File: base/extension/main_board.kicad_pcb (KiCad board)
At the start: 2 copper layers, 66.5 x 44 mm, 60 parts, among them IC1 TMC2209-LA-T, IC2 TMC2209-LA-T, IC3 TMC2209-LA-T, J1 USB_C_Receptacle_USB2.0_16P, J2 Conn_02x20_Odd_Even, J3 2-1734248-0, J4 Conn_01x02, J5 2-1734248-0, U1 LM7805_TO263, U2 MCP1700T-3302E/TT, U3 CH224K

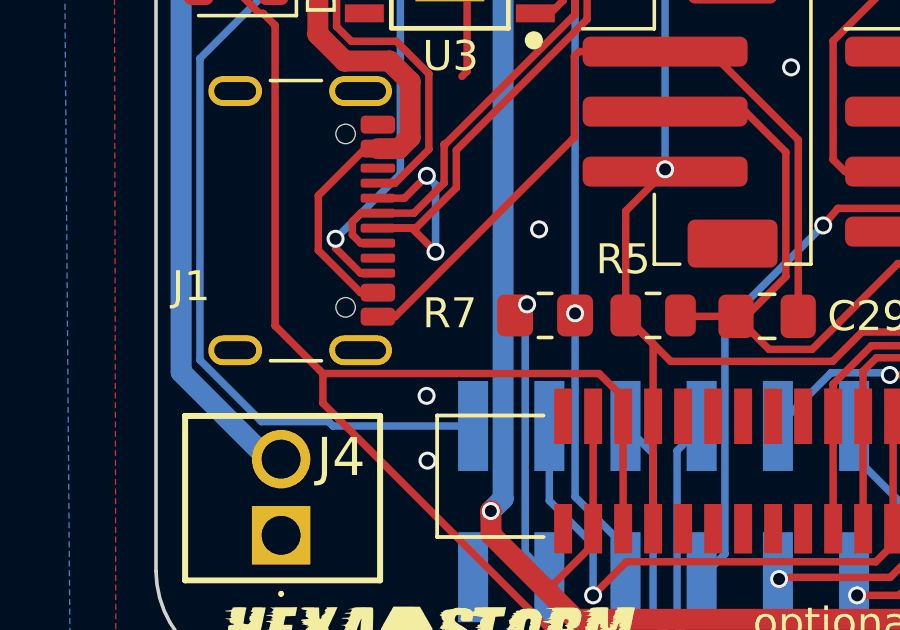
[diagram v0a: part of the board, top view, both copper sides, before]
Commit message: added mount felixprinter, standoffs
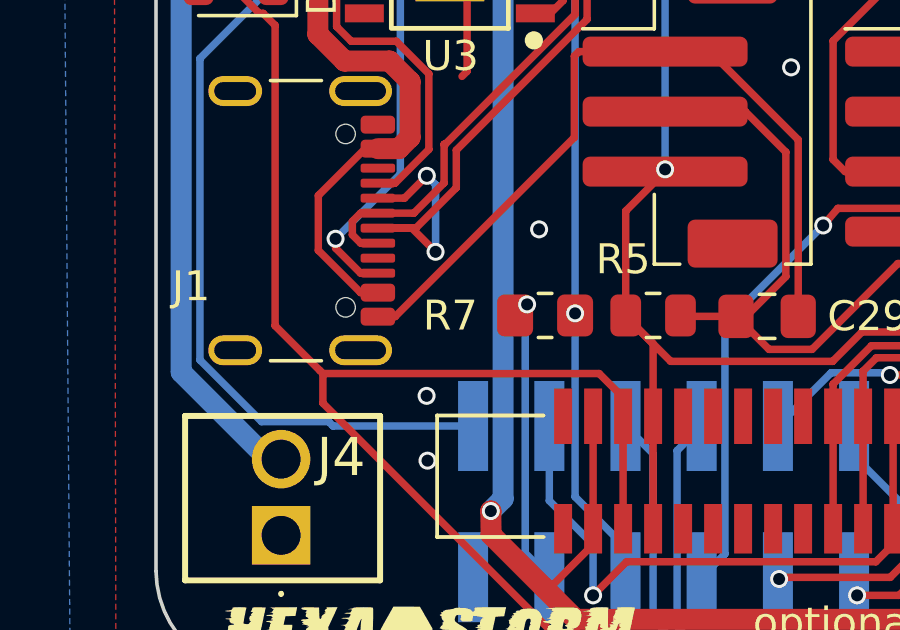
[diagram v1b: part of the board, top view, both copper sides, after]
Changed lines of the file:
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@@
 		(tags "resistor handsolder")
 		(property "Reference" "R7"
-			(at 3.18 0.07 180)
+			(at 3.16 -0.01 180)
 			(layer "F.SilkS")
 			(effects
